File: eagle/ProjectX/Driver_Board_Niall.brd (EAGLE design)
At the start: 100 x 100 mm, 192 parts, among them IC2 NCV78M05BDTRKG, J1 694102303002, J2 694102303002, U1 TC4427AEOA, U10 TC4427AEOA, U11 TC4427AEOA, U12 TC4427AEOA, U1200 CD74HC4067SM96, U13 TC4427AEOA, U14 TC4427AEOA, U15 TC4427AEOA, U16 TC4427AEOA, U17 TC4427AEOA, U18 TC4427AEOA, U19 TC4427AEOA, U2 TC4427AEOA, U20 TC4427AEOA, U200 ADA4091-2ARZ-RL, U21 TC4427AEOA, U22 TC4427AEOA, U23 TC4427AEOA, U24 TC4427AEOA, U25 TC4427AEOA, U26 TC4427AEOA, U27 TC4427AEOA, U28 TC4427AEOA, U29 TC4427AEOA, U3 TC4427AEOA, U30 TC4427AEOA, U31 TC4427AEOA, U32 TC4427AEOA, U33 TC4427AEOA, U34 TC4427AEOA, U35 TC4427AEOA, U36 TC4427AEOA, U37 TC4427AEOA, U38 TC4427AEOA, U39 TC4427AEOA, U4 TC4427AEOA, U40 TC4427AEOA, U41 TC4427AEOA, U42 TC4427AEOA, U43 TC4427AEOA, U44 TC4427AEOA, U45 TC4427AEOA, U46 TC4427AEOA, U47 TC4427AEOA, U48 TC4427AEOA, U49 TC4427AEOA, U5 TC4427AEOA, U50 TC4427AEOA, U6 TC4427AEOA, U7 TC4427AEOA, U8 TC4427AEOA, U9 TC4427AEOA

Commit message: More board work
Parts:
- moved DATA_2 36.2 mm to (40.7, 72.4)
- moved DATA_1 2.58 mm to (8.04, 56.1), turned to 180 degrees
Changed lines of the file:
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@@
 <attribute name="VALUE" x="49.73" y="88.54" size="1.27" layer="28" rot="MR180"/>
 </element>
-<element name="DATA_2" library="con-lstb" library_urn="urn:adsk.eagle:library:162" package="MA05-2" package3d_urn="urn:adsk.eagle:package:8329/1" value="" x="6.861" y="59.359">
-<attribute name="MF" value="" x="6.861" y="59.359" size="1.778" layer="27" display="off"/>
-<attribute name="MPN" value="" x="6.861" y="59.359" size="1.778" layer="27" display="off"/>
-<attribute name="NAME" x="0.511" y="62.28" size="1.27" layer="25" ratio="10"/>
-<attribute name="OC_FARNELL" value="unknown" x="6.861" y="59.359" size="1.778" layer="27" display="off"/>
-<attribute name="OC_NEWARK" value="unknown" x="6.861" y="59.359" size="1.778" layer="27" display="off"/>
-<attribute name="VALUE" x="6.861" y="55.168" size="1.27" layer="27" ratio="10"/>
+<element name="DATA_2" library="con-lstb" library_urn="urn:adsk.eagle:library:162" package="MA05-2" package3d_urn="urn:adsk.eagle:package:8329/1" value="" x="40.661" y="72.359">
+<attribute name="MF" value="" x="40.661" y="72.359" size="1.778" layer="27" display="off"/>
+<attribute name="MPN" value="" x="40.661" y="72.359" size="1.778" layer="27" display="off"/>
+<attribute name="NAME" x="34.311" y="75.28" size="1.27" layer="25" ratio="10"/>
+<attribute name="OC_FARNELL" value="unknown" x="40.661" y="72.359" size="1.778" layer="27" display="off"/>
+<attribute name="OC_NEWARK" value="unknown" x="40.661" y="72.359" size="1.778" layer="27" display="off"/>
+<attribute name="VALUE" x="40.661" y="68.168" size="1.27" layer="27" ratio="10"/>
 </element>
-<element name="DATA_1" library="con-lstb" library_urn="urn:adsk.eagle:library:162" package="MA05-2" package3d_urn="urn:adsk.eagle:package:8329/1" value="" x="6.862" y="53.803">
-<attribute name="MF" value="" x="6.862" y="53.803" size="1.778" layer="27" display="off"/>
-<attribute name="MPN" value="" x="6.862" y="53.803" size="1.778" layer="27" display="off"/>
-<attribute name="NAME" x="0.512" y="56.724" size="1.27" layer="25" ratio="10"/>
-<attribute name="OC_FARNELL" value="unknown" x="6.862" y="53.803" size="1.778" layer="27" display="off"/>
-<attribute name="OC_NEWARK" value="unknown" x="6.862" y="53.803" size="1.778" layer="27" display="off"/>
-<attribute name="VALUE" x="6.862" y="49.612" size="1.27" layer="27" ratio="10"/>
+<element name="DATA_1" library="con-lstb" library_urn="urn:adsk.eagle:library:162" package="MA05-2" package3d_urn="urn:adsk.eagle:package:8329/1" value="" x="8.038" y="56.097" rot="R180">
+<attribute name="MF" value="" x="8.038" y="56.097" size="1.778" layer="27" rot="R180" display="off"/>
+<attribute name="MPN" value="" x="8.038" y="56.097" size="1.778" layer="27" rot="R180" display="off"/>
+<attribute name="NAME" x="14.388" y="53.176" size="1.27" layer="25" ratio="10" rot="R180"/>
+<attribute name="OC_FARNELL" value="unknown" x="8.038" y="56.097" size="1.778" layer="27" rot="R180" display="off"/>
+<attribute name="OC_NEWARK" value="unknown" x="8.038" y="56.097" size="1.778" layer="27" rot="R180" display="off"/>
+<attribute name="VALUE" x="8.038" y="60.288" size="1.27" layer="27" ratio="10" rot="R180"/>
 </element>
 <element name="LED_3" library="SnapEDA-Library (5)" package="FCI_1655" value="1655" x="-10.19" y="32.1" rot="R270">

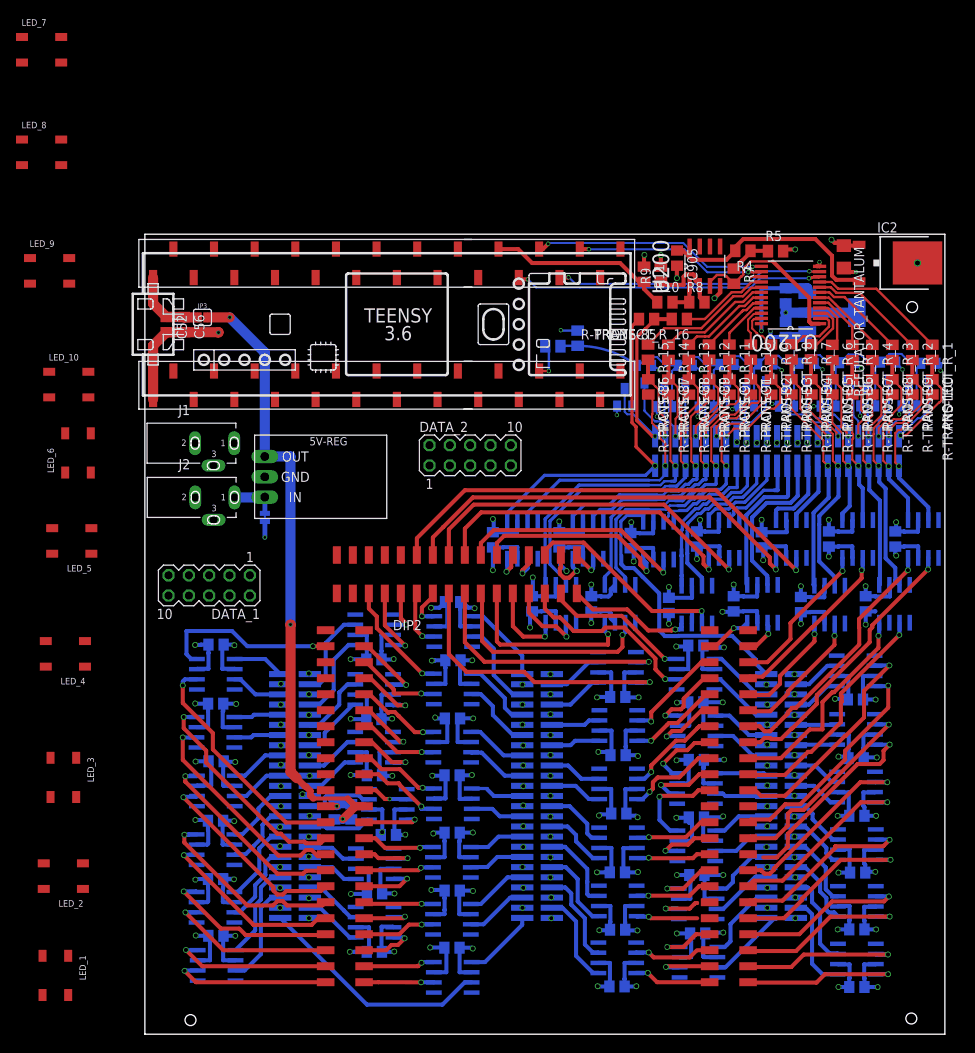
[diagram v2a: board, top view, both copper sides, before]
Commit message: Niall driver board finished draft 1
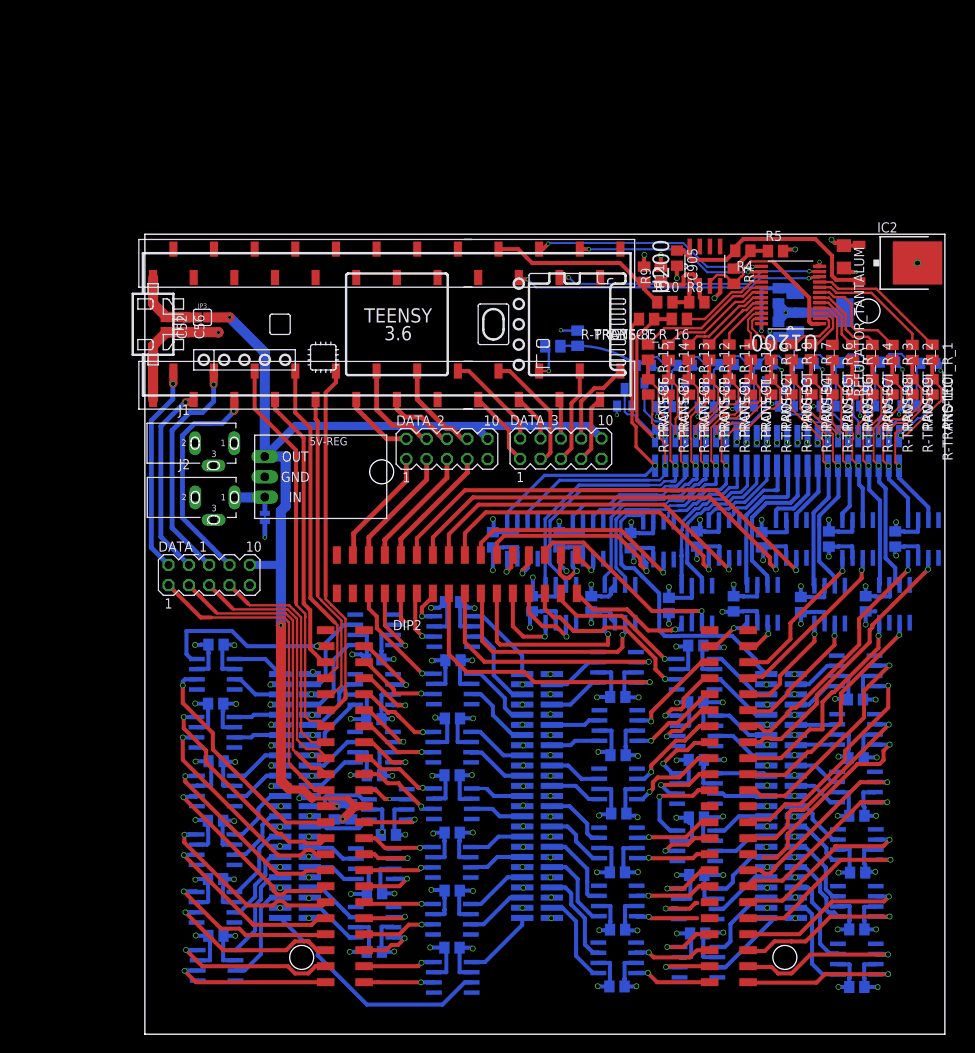
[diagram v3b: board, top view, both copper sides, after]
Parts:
- removed LED_1, LED_10, LED_2, LED_3, LED_4, LED_5, LED_6, LED_7, LED_8, LED_9: 1655, SnapEDA-Library (5):FCI_1655
- added DATA_3: (no value), con-lstb:MA05-2
- moved DATA_2 3.01 mm to (37.8, 73.2)
- moved UA78M05CDCY 1.50 mm to (84.4, 90.2)
- moved DATA_1 1.30 mm to (8.04, 57.4), turned to 0 degrees
- moved C53 0.90 mm to (79.2, 88.1)
- moved C54 0.90 mm to (79.2, 92.3)
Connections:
- removed net N$13: LED_2.2, LED_3.4
- removed net N$15: LED_3.2, LED_4.4
- removed net N$16: LED_4.2, LED_5.4
- removed net N$17: LED_5.2, LED_6.4
- removed net N$18: LED_6.2, LED_7.4
- removed net N$19: LED_7.2, LED_8.4
- removed net N$20: LED_8.2, LED_9.4
- removed net N$21: LED_10.4, LED_9.2
- removed net N$22: LED_1.4, U$1.6
- removed net N$9: LED_1.2, LED_2.4
- new net FPGA_1: DATA_1.1, DIP2.35
- new net FPGA_10: DATA_2.7, DIP2.197
- new net FPGA_11: DATA_2.5, DIP2.200
- new net FPGA_12: DATA_2.3, DIP2.203
- new net FPGA_13: DATA_2.1, DIP2.2
- new net FPGA_2: DATA_1.3, DIP2.33
- new net FPGA_3: DATA_1.5, DIP2.30
- new net FPGA_4: DATA_1.7, DIP2.28
- new net TEENSY_DATA_24: DATA_3.2, U$1.24
- new net TEENSY_DATA_25: DATA_3.1, U$1.25
- new net TEENSY_DATA_26: DATA_3.3, U$1.26
- new net TEENSY_DATA_27: DATA_3.4, U$1.27
- new net TEENSY_DATA_29: DATA_3.6, U$1.29
- new net TEENSY_DATA_30: DATA_3.5, U$1.30
- new net TEENSY_DATA_6: DIP2.15, U$1.6
- net +5V: now also DATA_1.10, DATA_2.10, DATA_3.10; no longer LED_1.1, LED_10.1, LED_2.1, LED_3.1, LED_4.1, LED_5.1, LED_6.1, LED_7.1, LED_8.1, LED_9.1
- net GND: now also DATA_1.9, DATA_2.9, DATA_3.9; no longer LED_1.3, LED_10.3, LED_2.3, LED_3.3, LED_4.3, LED_5.3, LED_6.3, LED_7.3, LED_8.3, LED_9.3
- net TEENSY_DATA_0: now also DATA_1.2
- net TEENSY_DATA_1: now also DATA_1.4
- net TEENSY_DATA_10: now also DATA_2.4
- net TEENSY_DATA_11: now also DATA_2.6
- net TEENSY_DATA_12: now also DATA_2.8
- net TEENSY_DATA_2: now also DATA_1.6
- net TEENSY_DATA_3: now also DATA_1.8
- net TEENSY_DATA_31: now also DATA_3.7
- net TEENSY_DATA_32: now also DATA_3.8
- net TEENSY_DATA_4: now also DIP2.24
- net TEENSY_DATA_5: now also DIP2.11
- net TEENSY_DATA_7: now also DIP2.18
- net TEENSY_DATA_8: now also DIP2.22
- net TEENSY_DATA_9: now also DATA_2.2
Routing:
- net +5V: track 81.3 -> 133.0 mm
- net TEENSY_DATA_4: track 0.00 -> 49.1 mm
- net FPGA_1: track 0.00 -> 46.3 mm
- net TEENSY_DATA_8: track 0.00 -> 45.6 mm
- net TEENSY_DATA_6: track 0.00 -> 45.6 mm
- net TEENSY_DATA_7: track 0.00 -> 39.5 mm
- net FPGA_2: track 0.00 -> 36.3 mm
- net TEENSY_DATA_5: track 0.00 -> 35.6 mm
- net FPGA_3: track 0.00 -> 32.5 mm
- net TEENSY_DATA_2: track 0.00 -> 29.3 mm, vias 0 -> 1
- net TEENSY_DATA_3: track 0.00 -> 28.8 mm, vias 0 -> 1
- net FPGA_4: track 0.00 -> 28.5 mm
- net TEENSY_DATA_0: track 0.00 -> 26.3 mm, vias 0 -> 1
- net TEENSY_DATA_1: track 0.00 -> 24.3 mm, vias 0 -> 1
- net FPGA_10: track 0.00 -> 15.4 mm
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
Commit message: More work
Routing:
- net TEENSY_DATA_6: track 45.6 -> 41.2 mm
- net VDD: track 325.7 -> 322.6 mm
- net 64: track 5.91 -> 7.50 mm
- net 25: track 7.68 -> 9.24 mm
- net TEENSY_DATA_3: track 28.8 -> 27.7 mm
- net 73: track 25.1 -> 26.0 mm
- net TO_TRAN_48: track 7.57 -> 8.31 mm

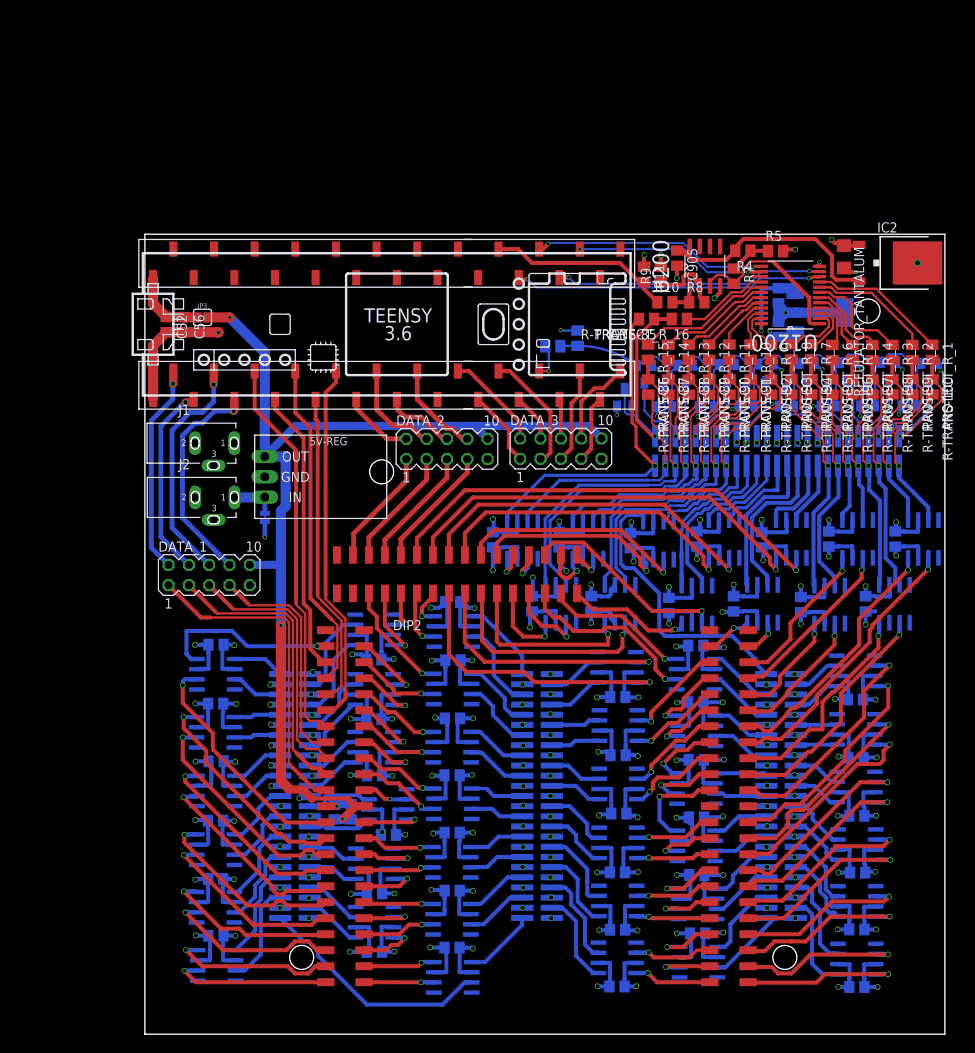
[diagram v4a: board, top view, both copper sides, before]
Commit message: Niall DRC errors fixed
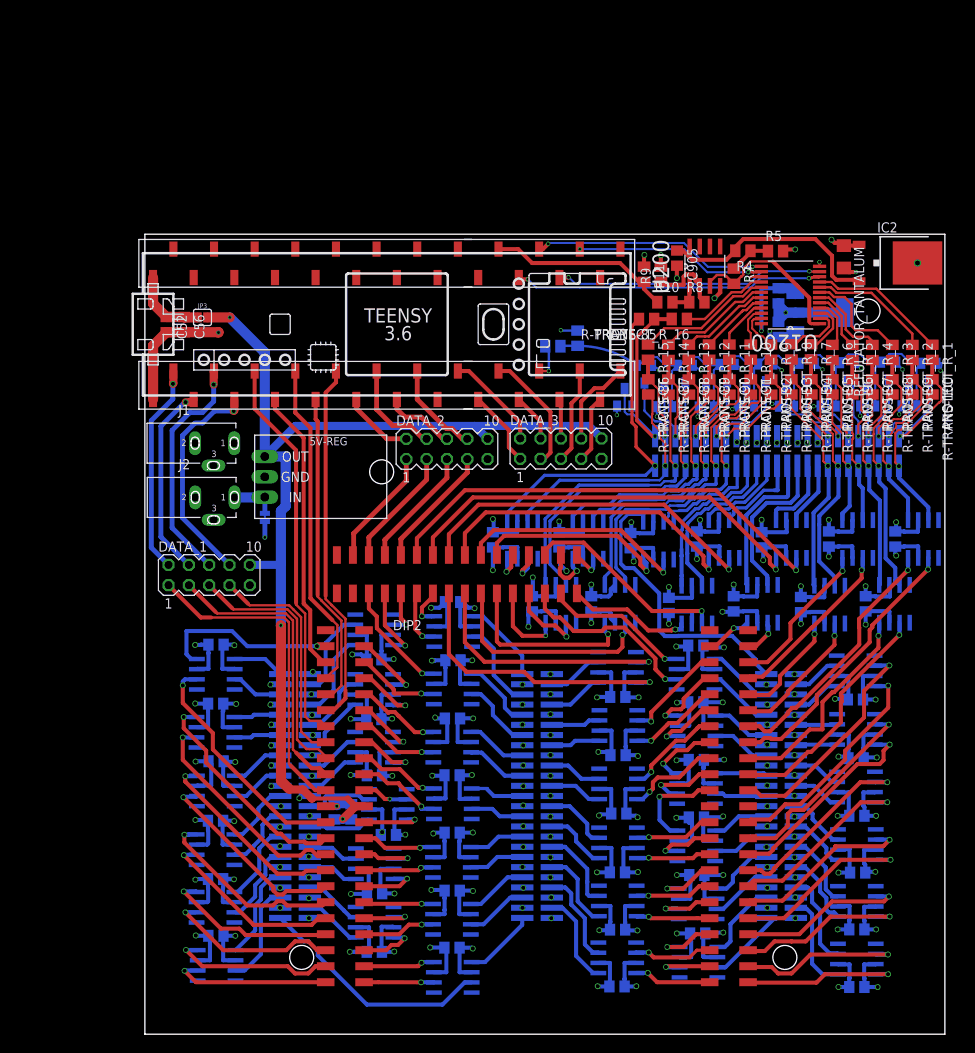
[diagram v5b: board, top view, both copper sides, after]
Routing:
- net GND: track 387.4 -> 400.0 mm
- net TO_TRAN_75: track 41.3 -> 36.3 mm
- net VDD: track 322.6 -> 321.1 mm

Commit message: Niall almost done
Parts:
- added TP1, TP10, TP11, TP12, TP13, TP14, TP15, TP16, TP17, TP18, TP19, TP2, TP20, TP3, TP4, TP5, TP6, TP7, TP8, TP9: TPSQPAD1-13Y, testpad:P1-13Y
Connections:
- new net N$13: TP2.TP, U$1.23/A3
- new net N$15: TP3.TP, U$1.22/A3
- new net N$16: TP4.TP, U$1.21/A3
- new net N$17: TP5.TP, U$1.20/A3
- new net N$18: TP6.TP, U$1.19/A5/SCL3
- new net N$19: TP7.TP, U$1.17/A4
- new net N$20: TP8.TP, U$1.18/A4/SDA3
- new net N$21: TP9.TP, U$1.16/A4
- new net N$22: TP10.TP, U$1.15/A4
- new net N$26: TP11.TP, U$1.14/A3
- new net N$27: TP12.TP, U$1.13/SCK3
- new net N$28: TP13.TP, U$1.GND7
- new net N$29: TP14.TP, U$1.A22/DAC1
- new net N$30: TP15.TP, U$1.A21/DAC0
- new net N$31: TP16.TP, U$1.3V4
- new net N$33: TP17.TP, U$1.AGND3
- new net N$9: TP1.TP, U$1.3V3_LO3
- net +5V: now also TP18.TP
- net GND: now also TP19.TP
- net VDD: now also TP20.TP
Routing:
- net +5V: track 133.3 -> 138.7 mm
- net N$30: track 0.00 -> 3.03 mm
- net N$28: track 0.00 -> 3.03 mm
- net N$26: track 0.00 -> 3.03 mm
- net N$21: track 0.00 -> 3.02 mm
- net N$20: track 0.00 -> 3.02 mm
- net N$17: track 0.00 -> 3.02 mm
- net N$9: track 0.00 -> 3.02 mm
- net N$15: track 0.00 -> 3.02 mm
- net N$31: track 0.00 -> 2.96 mm
- net N$29: track 0.00 -> 2.92 mm
- net N$27: track 0.00 -> 2.92 mm
- net N$22: track 0.00 -> 2.92 mm
- net N$19: track 0.00 -> 2.91 mm
- net N$18: track 0.00 -> 2.91 mm
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- removed copper zone on layer 3, net $VDD
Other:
- board text added: "5V"
- board text added: "<-POT"
- board text added: "GND"
- board text added: "VDD"

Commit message: V0 of driver board needs checked
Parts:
- added TP21, TP22, TP23, TP24, TP25, TP26, TP27, TP28, TP29, TP30, TP31, TP32, TP33, TP34, TP35, TP36, TP37, TP38, TP39, TP40, TP41: TPSQPAD1-13Y, testpad:P1-13Y
- DATA_1, DATA_2, DATA_3: device con-lstb:MA05-2 -> Pin_headers:MA05-2
- moved TP18 1.10 mm to (16.4, 91.1)
- moved TP20 1.00 mm to (22.1, 91.0)
- moved TP19 1.00 mm to (19.2, 91.0)
- moved DATA_2 0.73 mm to (37.6, 72.5)
- moved DATA_3 0.73 mm to (51.8, 72.5)
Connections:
- net 65: now also TP25.TP
- net 66: now also TP24.TP
- net 69: now also TP30.TP
- net 70: now also TP29.TP
- net GND: now also TP26.TP, TP31.TP
- net N$1: now also TP35.TP
- net N$3: now also TP36.TP
- net N$32: now also TP37.TP
- net N$5: now also TP21.TP
- net TEENSY_DATA_4: now also TP34.TP
- net TEENSY_DATA_5: now also TP41.TP
- net TEENSY_DATA_6: now also TP40.TP
- net TEENSY_DATA_7: now also TP39.TP
- net TEENSY_DATA_8: now also TP38.TP
- net TO_TRAN_65: now also TP23.TP
- net TO_TRAN_66: now also TP22.TP
- net TO_TRAN_69: now also TP27.TP
- net TO_TRAN_70: now also TP28.TP
- net VDD: now also TP32.TP, TP33.TP
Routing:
- net TO_TRAN_70: track 7.41 -> 24.1 mm, vias 0 -> 1
- net TO_TRAN_65: track 12.3 -> 27.7 mm, vias 0 -> 1
- net TO_TRAN_69: track 7.41 -> 21.4 mm, vias 0 -> 1
- net TO_TRAN_66: track 11.9 -> 25.1 mm, vias 0 -> 1
- net 70: track 22.8 -> 33.0 mm
- net 66: track 20.4 -> 27.6 mm
- net N$5: track 23.2 -> 30.3 mm
- net TEENSY_DATA_7: track 39.5 -> 46.4 mm
- net 69: track 22.8 -> 29.4 mm
- net 65: track 19.5 -> 24.6 mm
- net TEENSY_DATA_5: track 35.6 -> 40.1 mm, vias 0 -> 1
- net N$1: track 17.3 -> 21.3 mm
- net TEENSY_DATA_8: track 45.6 -> 49.4 mm
- net N$32: track 21.6 -> 25.4 mm
- net TEENSY_DATA_4: track 48.9 -> 52.6 mm
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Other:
- board text added: "+"
- board text added: "+5V"
- board text added: "-"
- board text added: "0"
- board text added: "1"
- board text added: "10"
- board text added: "11"
- board text added: "12"
- board text added: "197"
- board text added: "2"
- board text added: "200"
- board text added: "203"
- board text added: "24"
- board text added: "25"
- board text added: "26"
- board text added: "27"
- board text added: "28"
- board text added: "29"
- board text added: "3"
- board text added: "3.3V"
- board text added: "30"
- board text added: "31"
- board text added: "32"
- board text added: "33"
- board text added: "35"
- board text added: "9"
- board text added: "<- Out Mux"
- board text added: "Amplified Signal"
- board text added: "FPGA PINS"
- board text added: "In Mux T00"
- board text added: "In Mux T01"
- board text added: "POT"
- board text added: "T00"
- board text added: "T01"
- board text added: "T02"
- board text added: "T03"
- board text added: "T04"
- board text added: "T05"
- board text added: "T06"
- board text added: "T07"
- board text added: "T08"
- board text added: "T09"
- board text added: "T10"
- board text added: "T11"
- board text added: "T12"
- board text added: "T13"
- board text added: "T14"
- board text added: "T15"
- board text added: "T16"
- board text added: "T17"
- board text added: "T18"
- board text added: "T19"
- board text added: "T20"
- board text added: "T21"
- board text added: "T22"
- board text added: "T23"
- board text added: "T24"
- board text added: "T25"
- board text added: "T26"
- board text added: "T27"
- board text added: "T28"
- board text added: "T29"
- board text added: "T30"
- board text added: "T31"
- board text added: "T32"
- board text added: "T33"
- board text added: "T34"
- board text added: "T35"
- board text added: "T36"
- board text added: "T37"
- board text added: "T38"
- board text added: "T39"
- board text added: "T40"
- board text added: "T41"
- board text added: "T42"
- board text added: "T43"
- board text added: "T44"
- board text added: "T45"
- board text added: "T46"
- board text added: "T47"
- board text added: "T48"
- board text added: "T49"
- board text added: "T50"
- board text added: "T51"
- board text added: "T52"
- board text added: "T53"
- board text added: "T54"
- board text added: "T55"
- board text added: "T56"
- board text added: "T57"
- board text added: "T58"
- board text added: "T59"
- board text added: "T60"
- board text added: "T61"
- board text added: "T62"
- board text added: "T63"
- board text added: "T64"
- board text added: "T65"
- board text added: "T66"
- board text added: "T67"
- board text added: "T68"
- board text added: "T69"
- board text added: "T70"
- board text added: "T71"
- board text added: "T72"
- board text added: "T73"
- board text added: "T74"
- board text added: "T75"
- board text added: "T76"
- board text added: "T77"
- board text added: "T78"
- board text added: "T79"
- board text added: "T80"
- board text added: "T81"
- board text added: "T82"
- board text added: "T83"
- board text added: "T84"
- board text added: "T85"
- board text added: "T86"
- board text added: "T87"
- board text added: "T88"
- board text added: "T89"
- board text added: "T90"
- board text added: "T91"
- board text added: "T92"
- board text added: "T93"
- board text added: "T94"
- board text added: "T95"
- board text added: "T96"
- board text added: "T97"
- board text added: "T98"
- board text added: "T99"
- board text added: "T:4 F:24"
- board text added: "T:5 F:11"
- board text added: "T:6 F:15"
- board text added: "T:7 F:18"
- board text added: "T:8 F:22"
- board text added: "TRANSDUCER DRIVER BOARD V0 BY NIALL MACDONALD"
- board text added: "Teensy_PINS"
- board text added: "To D 38"
- board text added: "To D 40"
- board text added: "To D 46"
- board text added: "To D 48"
- board text added: "To T 38"
- board text added: "To T 40"
- board text added: "To T 46"
- board text added: "To T 48"

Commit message: Boards almost done
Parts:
- moved TP18 0.22 mm to (16.3, 90.9)
